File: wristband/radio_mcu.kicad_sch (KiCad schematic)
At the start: 17 parts, among them SW1 SOS, U3 NINA-B400, U4 DWM3000, Y1 32.768kHz

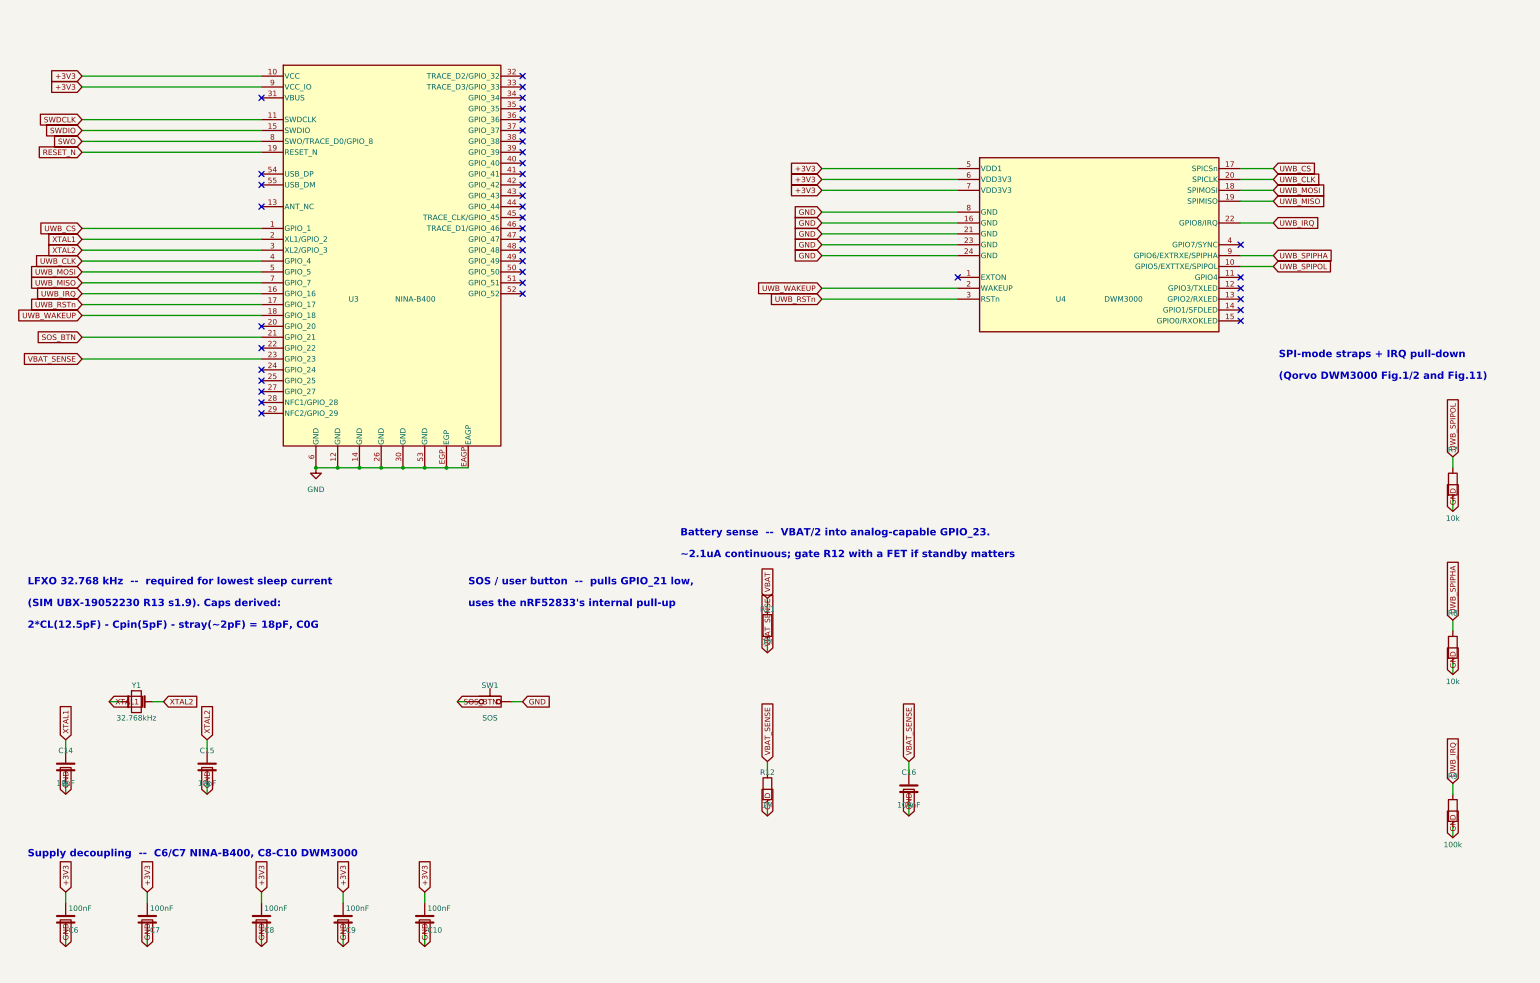
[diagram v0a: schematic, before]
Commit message: Convert global labels to power symbols; import footprints to PCB
Continues the ground cleanup from 0263e7f across the rest of the wristband
sheets: global labels replaced with explicit power symbols and wired
junctions, so connections are drawn rather than implied by name.

                     wires      labels      junctions   symbols
  power_bms          61 -> 83   61 -> 51    0 -> 3      25 -> 36
  programming_debug   7 ->  8    7 ->  4    0 -> 1       1 ->  3
  radio_mcu          71 -> 79   64 -> 42    7 -> 17     18 -> 32
  regulation          7 ->  7    7 ->  4    0 -> 0       3 ->  6

The added symbols are all power ports, so the BOM is untouched: still 47
components, 76 nets, 42 no-connects, 35 analyzer findings with 1 error --
identical before and after. The one error is the known DW01A false
positive (U1.6 GND sits on CELL_N by design, per the reference circuit).

Also ran Update PCB from Schematic on the wristband: 0 -> 46 footprints.
Nothing routed yet, no zones, board outline unchanged.

Co-Authored-By: Claude Opus 5 (1M context) <noreply@anthropic.com>
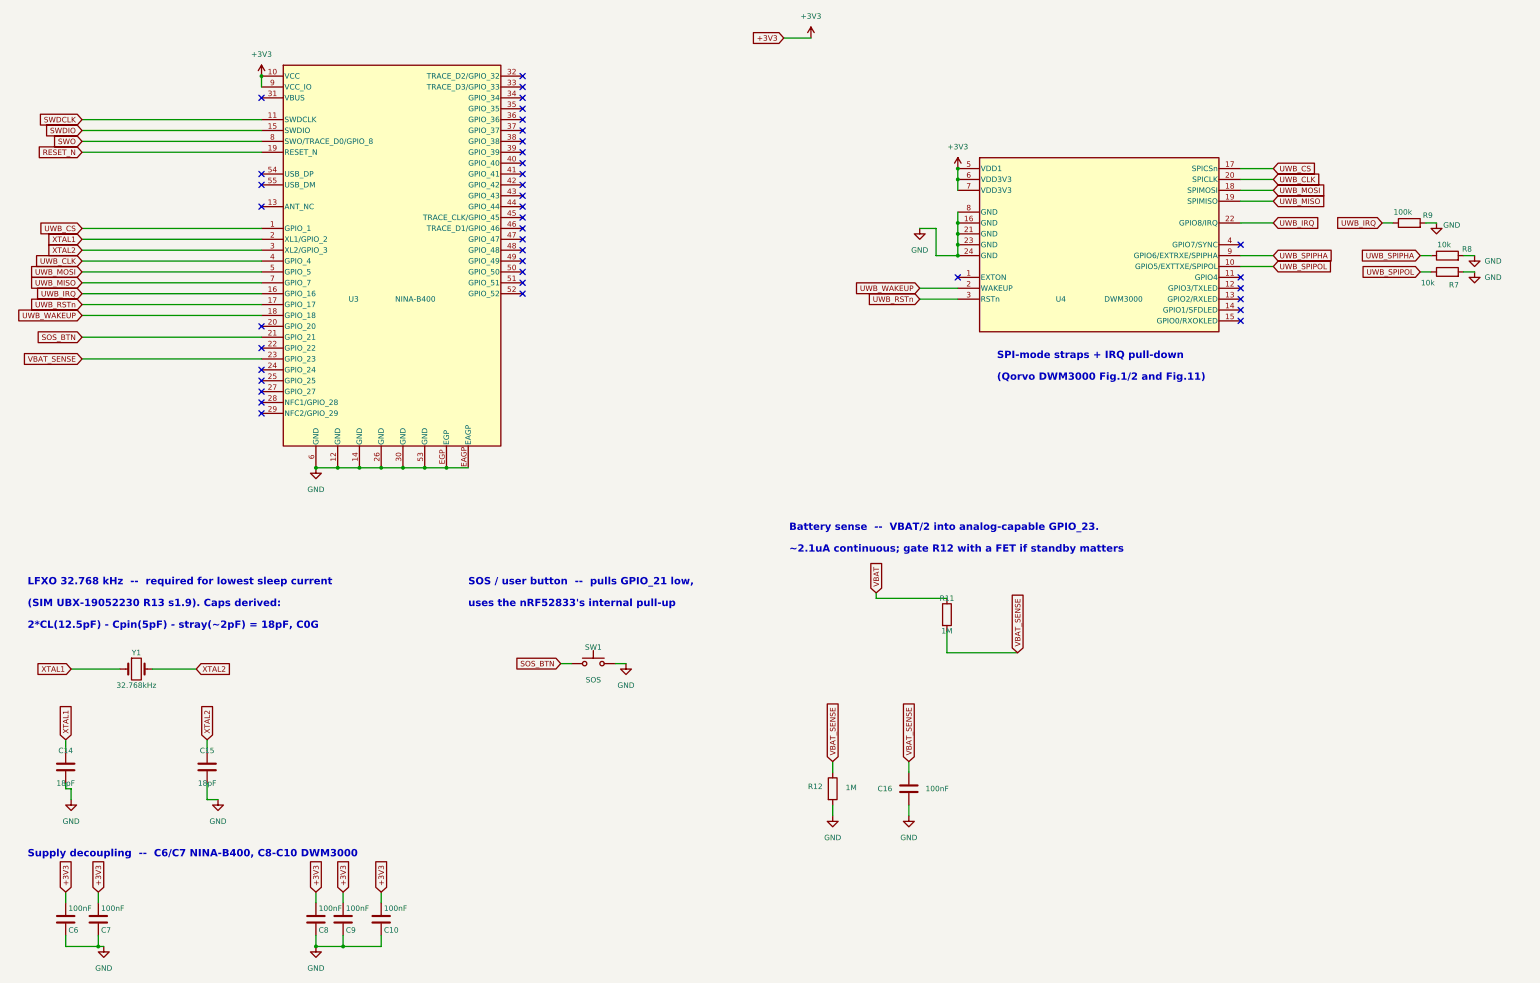
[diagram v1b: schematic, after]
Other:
- moved on the sheet: C10, C7, C8, R11, R12, R7, R8, R9, SW1, Y1

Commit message: Migrate wristband to DWM3001C; swap LDO to TPS7A02; fix ERC
Replace the NINA-B400 + DWM3000 pair with a single Qorvo DWM3001C, then
replace the MCP1700 LDO with a nanopower TI TPS7A0233. Wristband ERC goes
from 1 error / 13 warnings to 0 errors / 1 warning.

DWM3001C (U4), verified against Qorvo DS Rev B May 2022:
- Integrates DW3110 UWB + nRF52833 BLE MCU + LIS2DH12 + UWB antenna +
  Bluetooth chip antenna + 38.4MHz crystal. Its nRF52833 is now the host,
  so U3 (NINA-B400) is deleted.
- The DW3110<->nRF52833 SPI is internal, so the board-level UWB SPI bus,
  IRQ/RSTn/WAKEUP, the GPIO5/6 SPI-mode straps (R7/R8), the IRQ pulldown
  (R9) and the external LFXO (Y1/C14/C15) are all gone. C8-C10 too.
- AE1 (PRO-IS-237) removed: the module carries both antennas, so
  antenna.kicad_sch is documentation-only and places nothing.
- SWD moved for the first time: SWD_CLK=2, SWD_DIO=3, RESET=47 (P0.18),
  SWO=28 (P1.00). Battery sense moved to P0.02 = AIN0. Both P1.00=SWO and
  P0.02=AIN0 confirmed in nRF52833 PS v1.7 p825-826.
- Symbol + DWM3001C_PLACEHOLDER footprint are wristband-only, in libs/.
  The footprint has TWO unresolved dimensions (side pitch back-derives to
  1.06375mm; bottom pad row width undimensioned and apparently off-centre).
  VERIFY BEFORE FAB.

TPS7A0233PDBVR (U5), verified against TI SBVS277C:
- Iq 1.6uA typ / 4uA max -> 25nA typ / 46nA max; it was the largest single
  standby draw, bigger than the DWM3001C's own 850nA sleep. Board standby
  ~4.3uA -> ~2.7uA. Accuracy +/-1.5% vs +/-2.5%.
- Not a drop-in: SOT-23-5 1=IN 2=GND 3=EN 4=NC 5=OUT. EN ties to VBAT
  because TPS7A02 is disabled when EN floats and the MCU on this rail
  cannot enable its own supply.
- C12 1uF -> 2.2uF for the 0.5uF effective-capacitance stability floor.
- Symbol is self-contained: KiCad ships no TPS7A02, and every TPS7A05
  sibling is extends-based, which kicad-cli cannot load.

ERC fixes:
- Real bug: regulation.kicad_sch had no labels at all, so U5's input and
  C11 sat on an iso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
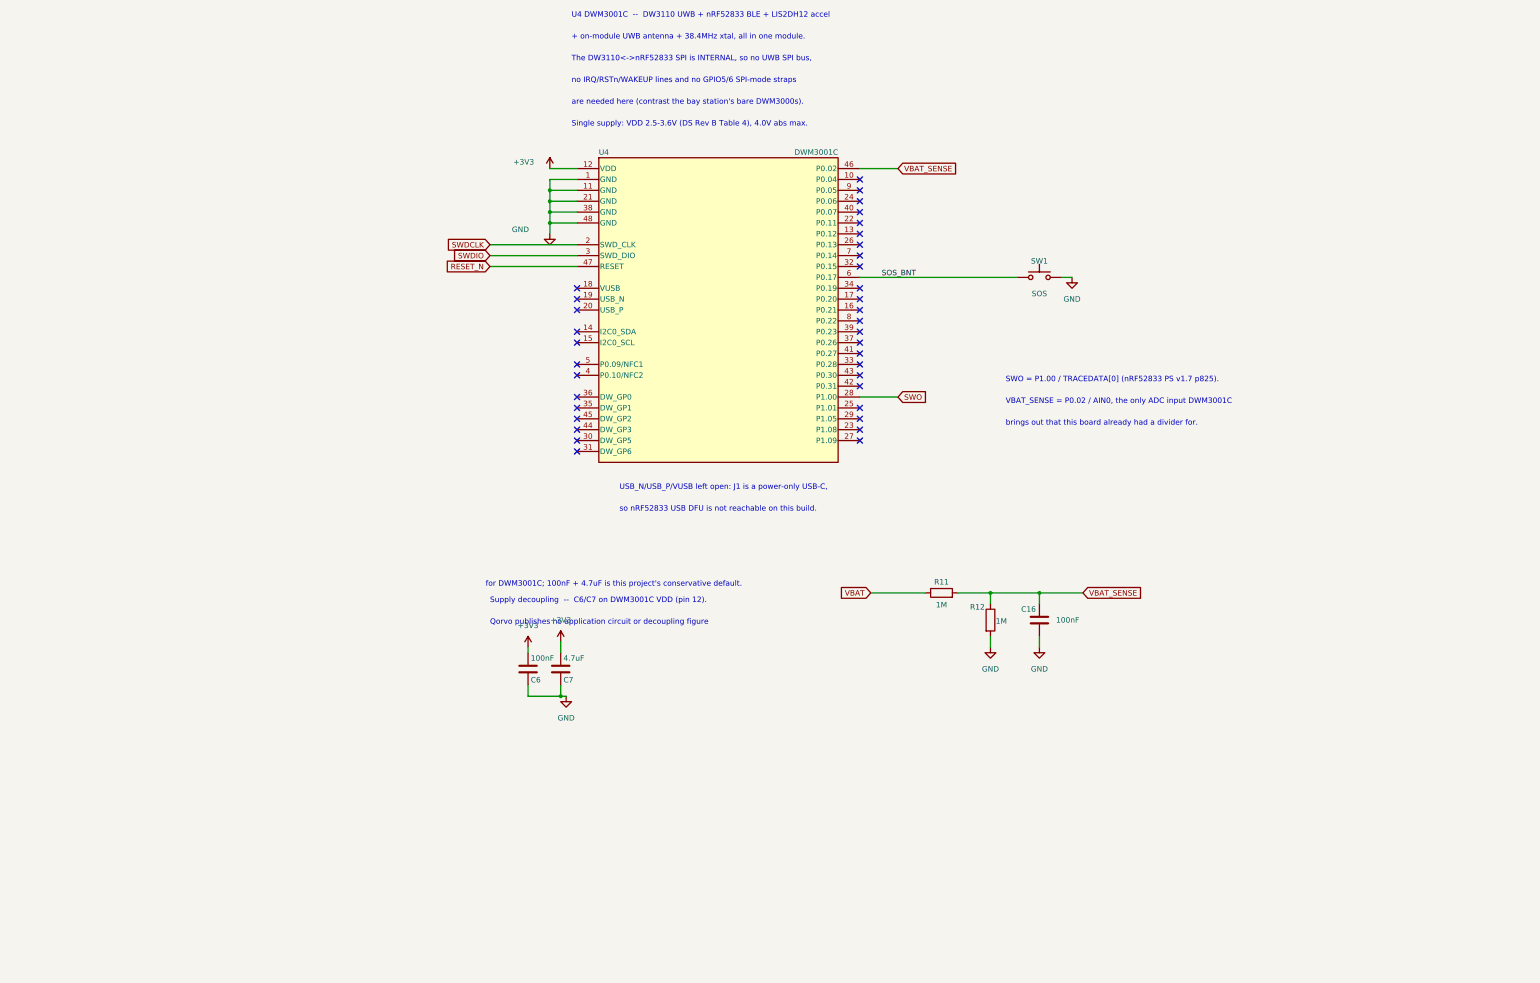
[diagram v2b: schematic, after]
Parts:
- removed C10, C8, C9: 100nF, Capacitor_SMD:C_0603_1608Metric, symbol Device:C
- removed C14, C15: 18pF, Capacitor_SMD:C_0603_1608Metric, symbol Device:C
- removed R7, R8: 10k, Resistor_SMD:R_0603_1608Metric, symbol Device:R
- removed R9: 100k, Resistor_SMD:R_0603_1608Metric, symbol Device:R
- removed U3: NINA-B400, wristband:NINA-B400-55_PLACEHOLDER, symbol wristband:NINA-B400
- removed U4: DWM3000, uwb_rescue_locator_shared:DWM3000_PLACEHOLDER, symbol uwb_rescue_locator_shared:DWM3000
- removed Y1: 32.768kHz, Crystal:Crystal_SMD_3215-2Pin_3.2x1.5mm, symbol Device:Crystal
- added U4: DWM3001C, wristband:DWM3001C_PLACEHOLDER, symbol wristband:DWM3001C
- C7: value 100nF -> 4.7uF
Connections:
- net +3V3: now also U4.12 (VDD)
- net GND: now also U4.1 (GND), U4.11 (GND), U4.21 (GND), U4.38 (GND), U4.48 (GND)
- net RESET_N: now also U4.47 (RESET)
- net SWDCLK: now also U4.2 (SWD_CLK)
- net SWDIO: now also U4.3 (SWD_DIO)
- net SWO: now also U4.28 (P1.00)
- net VBAT_SENSE: now also U4.46 (P0.02)
- net SOS_BTN renamed SOS_BNT
- net SOS_BNT: now also U4.6 (P0.17)
- no-connect marks 39 -> 36
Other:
- note added: "+ on-module UWB antenna + 38.4MHz xtal, all in one module."
- note added: "Qorvo publishes no application circuit or decoupling figure"
- note added: "SWO = P1.00 / TRACEDATA[0] (nRF52833 PS v1.7 p825)."
- note added: "Single supply: VDD 2.5-3.6V (DS Rev B Table 4), 4.0V abs max."
- note added: "Supply decoupling -- C6/C7 on DWM3001C VDD (pin 12)."
- note added: "The DW3110<->nRF52833 SPI is INTERNAL, so no UWB SPI bus,"
- note added: "U4 DWM3001C -- DW3110 UWB + nRF52833 BLE + LIS2DH12 accel"
- note added: "USB_N/USB_P/VUSB left open: J1 is a power-only USB-C,"
- note added: "VBAT_SENSE = P0.02 / AIN0, the only ADC input DWM3001C"
- note added: "are needed here (contrast the bay station's bare DWM3000s)."
- note added: "brings out that this board already had a divider for."
- note added: "for DWM3001C; 100nF + 4.7uF is this project's conservative default."
- note added: "no IRQ/RSTn/WAKEUP lines and no GPIO5/6 SPI-mode straps"
- note added: "so nRF52833 USB DFU is not reachable on this build."
- note removed: "(Qorvo DWM3000 Fig.1/2 and Fig.11)"
- note removed: "(SIM UBX-19052230 R13 s1.9). Caps derived:"
- note removed: "2*CL(12.5pF) - Cpin(5pF) - stray(~2pF) = 18pF, C0G"
- note removed: "Battery sense -- VBAT/2 into analog-capable GPIO_23."
- note removed: "LFXO 32.768 kHz -- required for lowest sleep current"
- note removed: "SOS / user button -- pulls GPIO_21 low,"
- note removed: "SPI-mode straps + IRQ pull-down"
- note removed: "Supply decoupling -- C6/C7 NINA-B400, C8-C10 DWM3000"
- note removed: "uses the nRF52833's internal pull-up"
- note removed: "~2.1uA continuous; gate R12 with a FET if standby matters"
- moved on the sheet: C16, C6, C7, R11, R12, SW1
